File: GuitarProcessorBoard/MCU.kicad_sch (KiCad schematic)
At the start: 94 parts, among them J301 SWD Header, J302 PWR, J303 TAP, J304 MODE, J305 BYP, J306 EXP, J307 ScopeGroundLoop, SW301 RST, SW302 BOOT, U301 STM32H7B0VBT6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

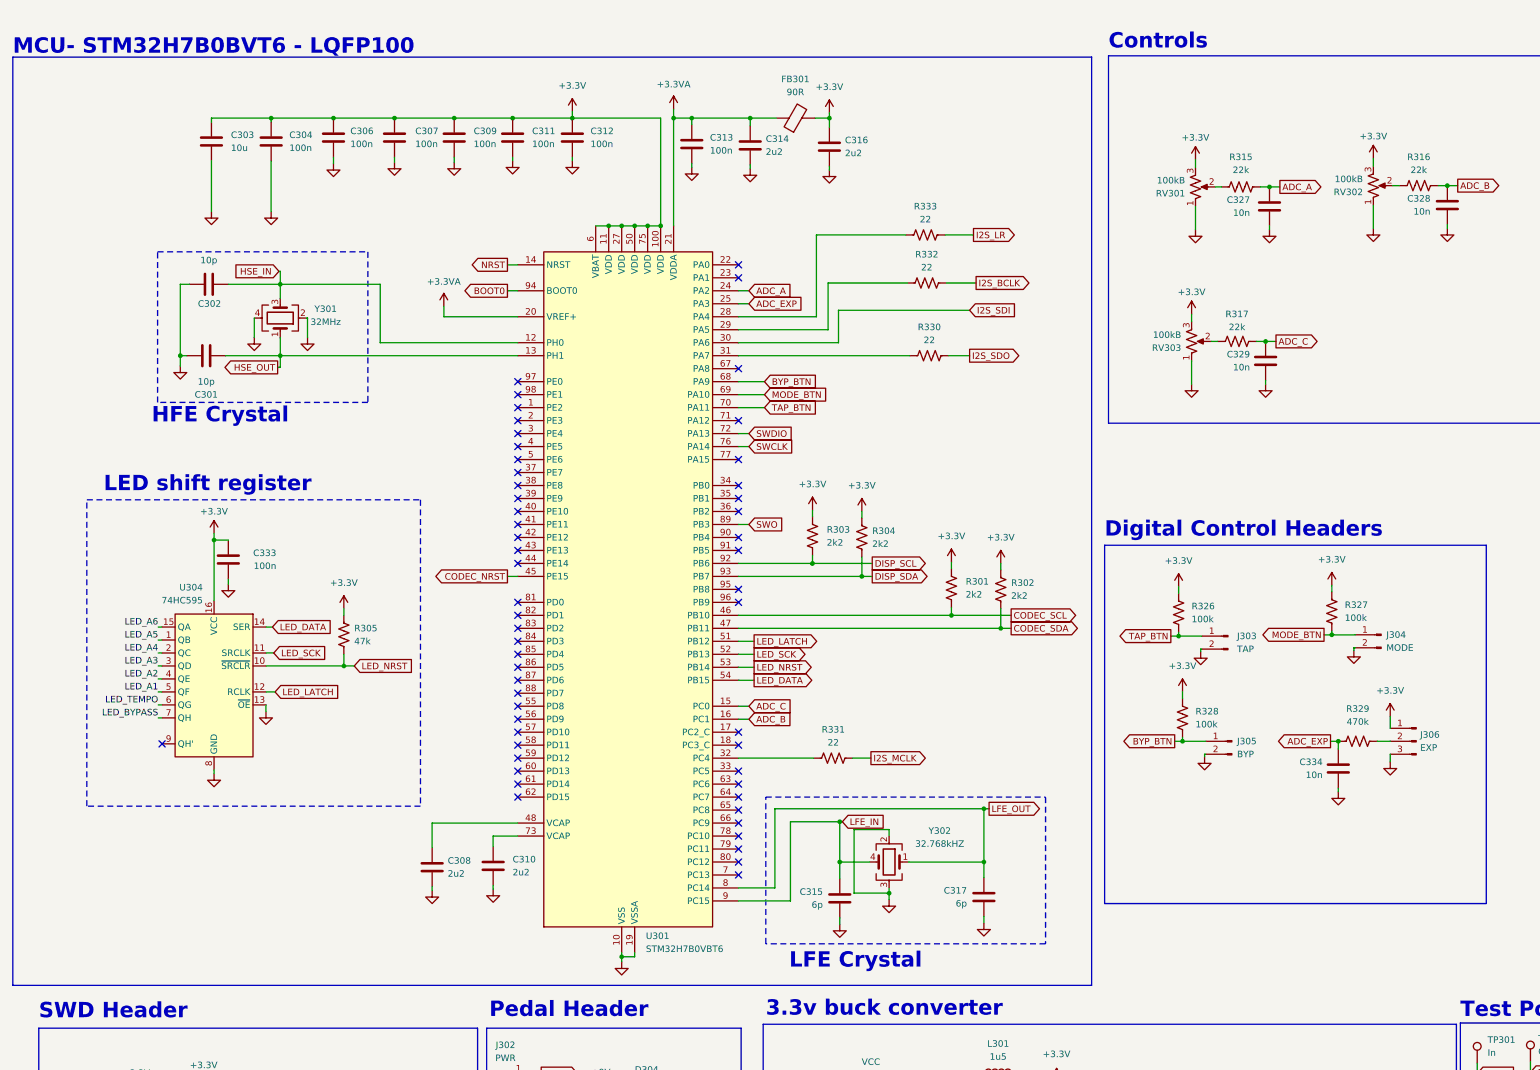
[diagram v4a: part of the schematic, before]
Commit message: differential output sim
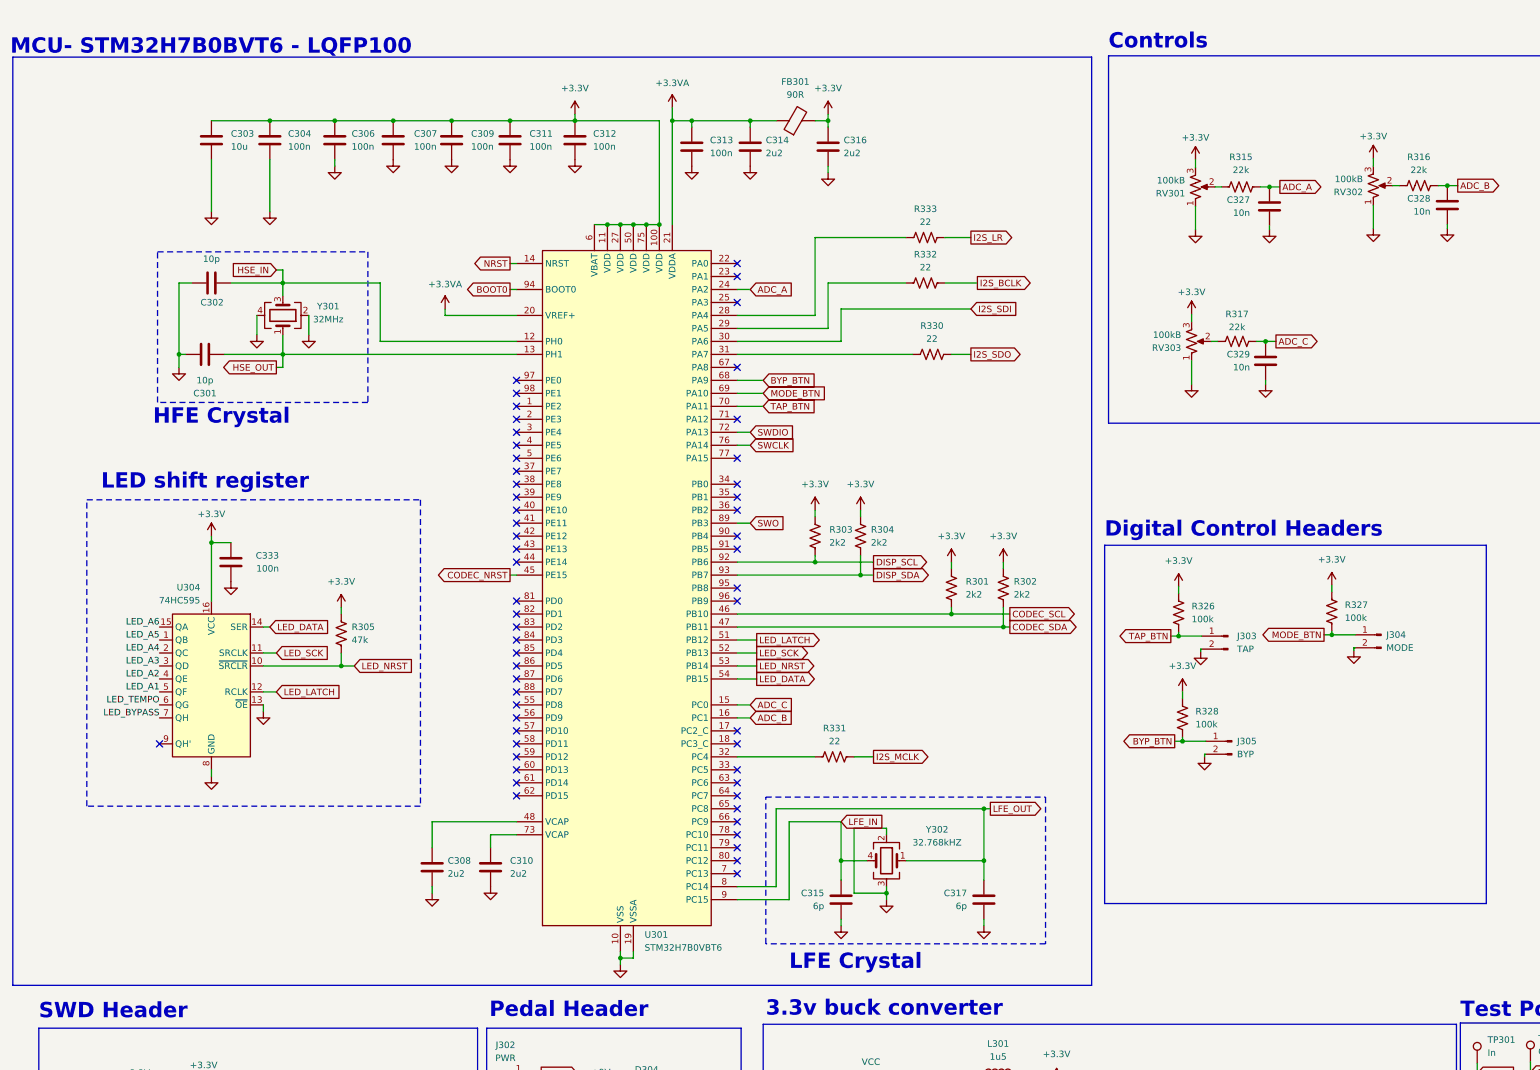
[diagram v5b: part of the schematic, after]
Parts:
- removed C334: 10n, Capacitor_SMD:C_0805_2012Metric, symbol Device:C
- removed J306: EXP, Connector_PinHeader_2.54mm:PinHeader_1x03_P2.54mm_Vertical, symbol Connector:Conn_01x03_Pin
- removed R329: 470k, Resistor_SMD:R_0805_2012Metric, symbol Device:R_US
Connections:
- net ADC_EXP: no longer names the net of U301.25 (PA3)
- no-connect marks 55 -> 56
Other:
- moved on the sheet: C302, C306, C307, C309, C310, C311, C312, C313, C317, C333, FB301, R302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

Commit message: routing start
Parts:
- removed D303: PMEG3030, Diode_SMD:D_SOD-123, symbol Device:D_Schottky
- removed J303: TAP, Connector_PinHeader_2.54mm:PinHeader_1x02_P2.54mm_Vertical, symbol Connector:Conn_01x02_Pin
- removed R326: 100k, Resistor_SMD:R_0805_2012Metric, symbol Device:R_US
- removed TP304: VCC, TestPoint:TestPoint_THTPad_D2.0mm_Drill1.0mm_VAL, symbol Connector:TestPoint
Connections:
- net +3.3V: now also J301.1 (Pin_1)
- net TAP_BTN: no longer names the net of U301.70 (PA11)
- no-connect marks 56 -> 57

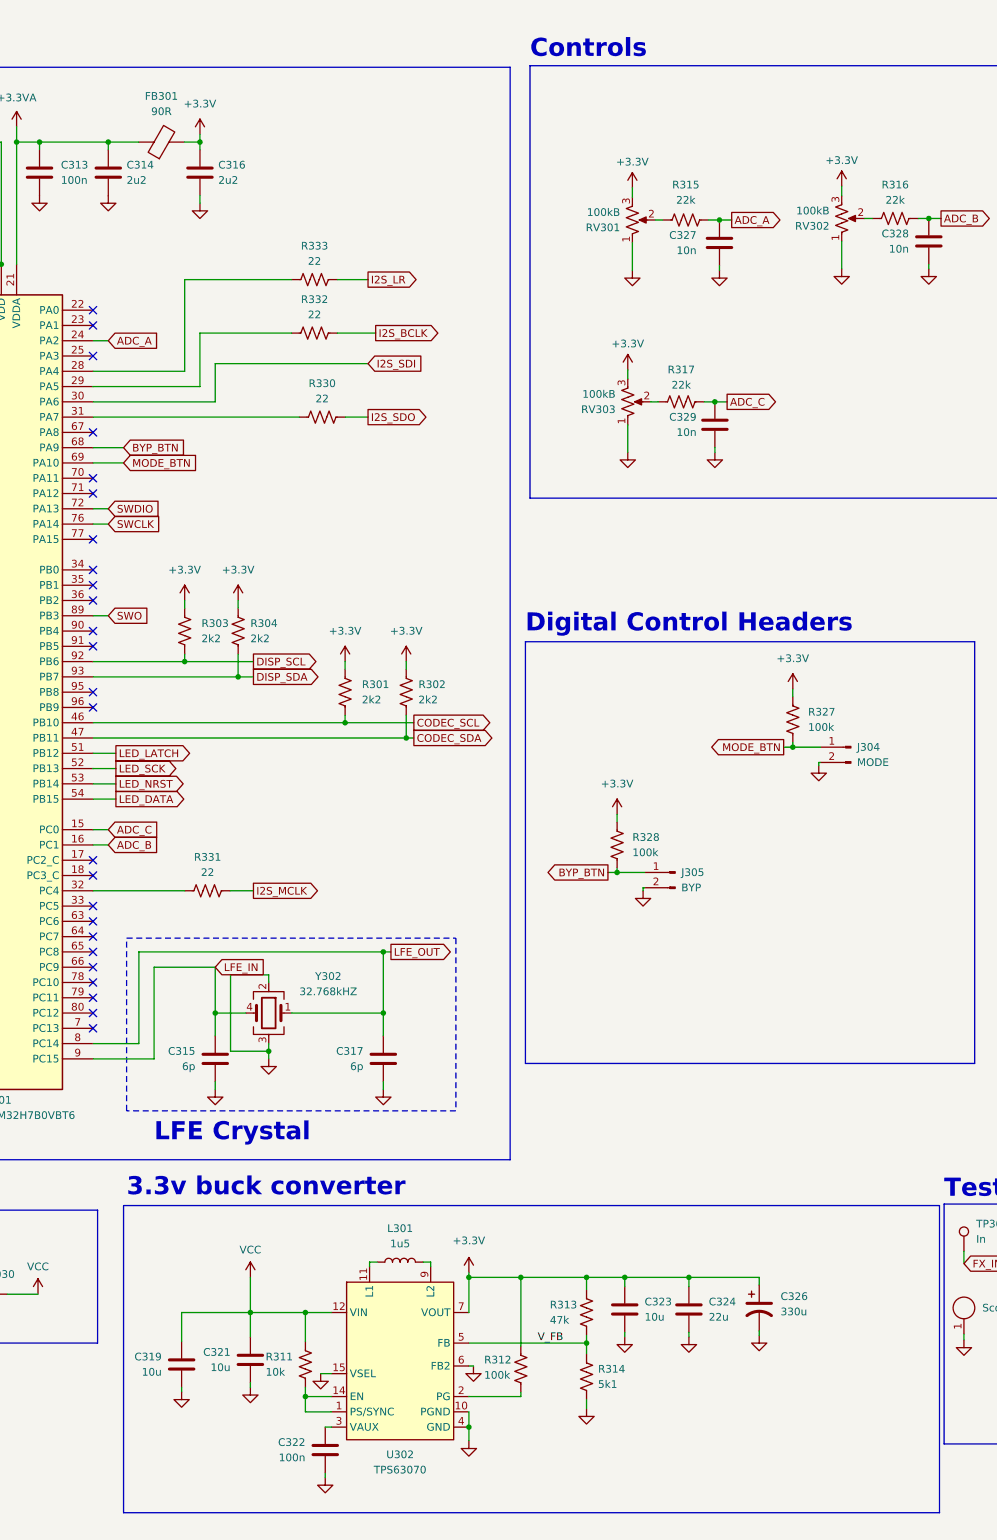
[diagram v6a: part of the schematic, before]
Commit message: more decoupling caps, return vias
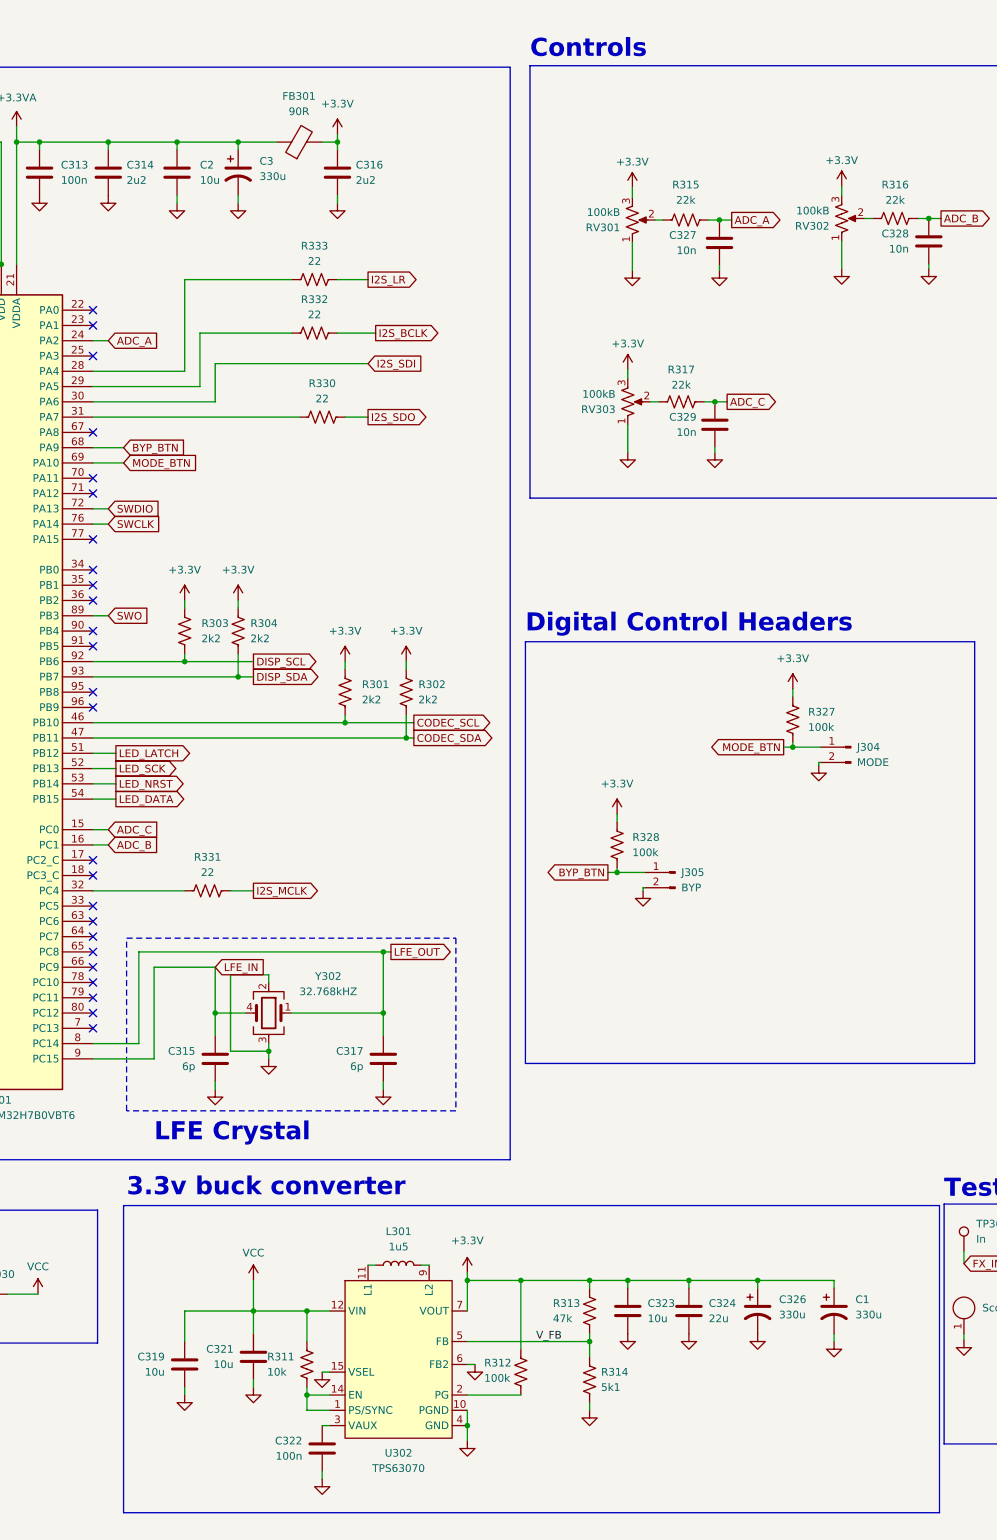
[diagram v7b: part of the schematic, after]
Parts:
- added C1, C3: 330u, Capacitor_THT:CP_Radial_D5.0mm_P2.50mm, symbol Device:C_Polarized_US
- added C2: 10u, Capacitor_SMD:C_0805_2012Metric, symbol Device:C
- U303: footprint Display:SSD1306_OLED_128x64 -> Display:SSD1306_OLED_128x64_OffBoard
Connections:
- net +3.3V: now also C1.1
- net +3.3VA: now also C2.1, C3.1
- net GND: now also C1.2, C2.2, C3.2
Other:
- moved on the sheet: C316, C319, C321, C322, C323, C326, FB301, L301, R312, R313, R314

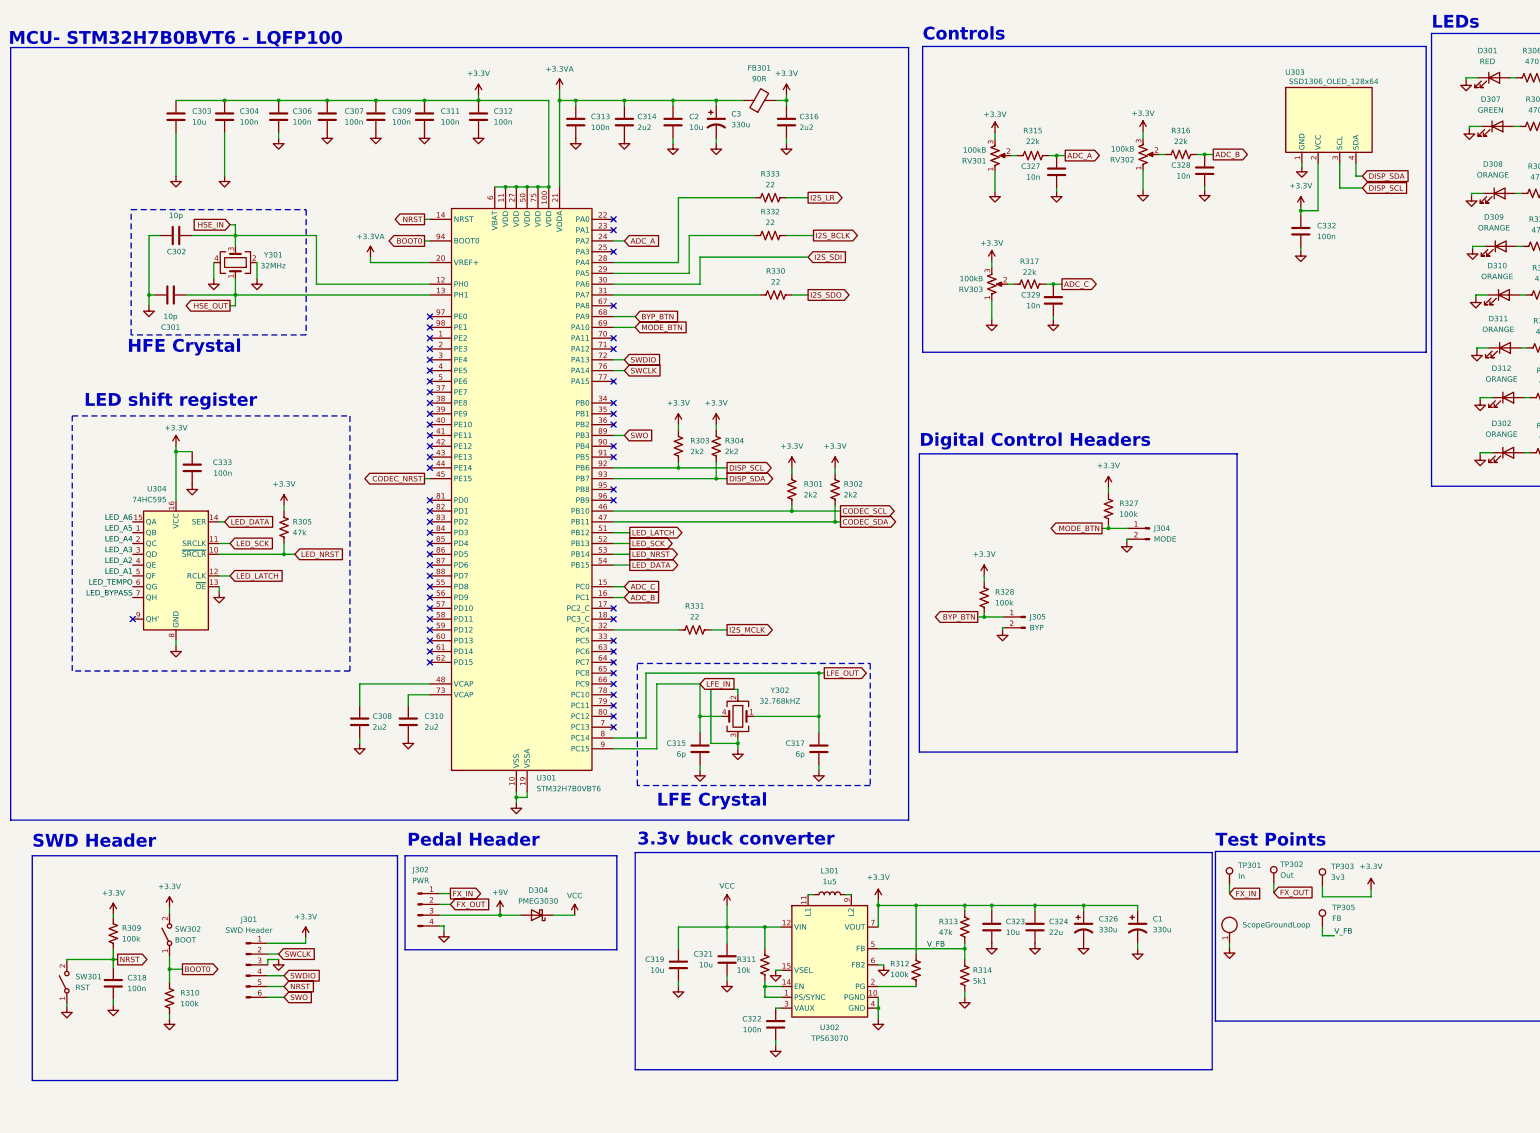
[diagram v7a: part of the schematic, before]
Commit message: split PSU schematic, DRC passing
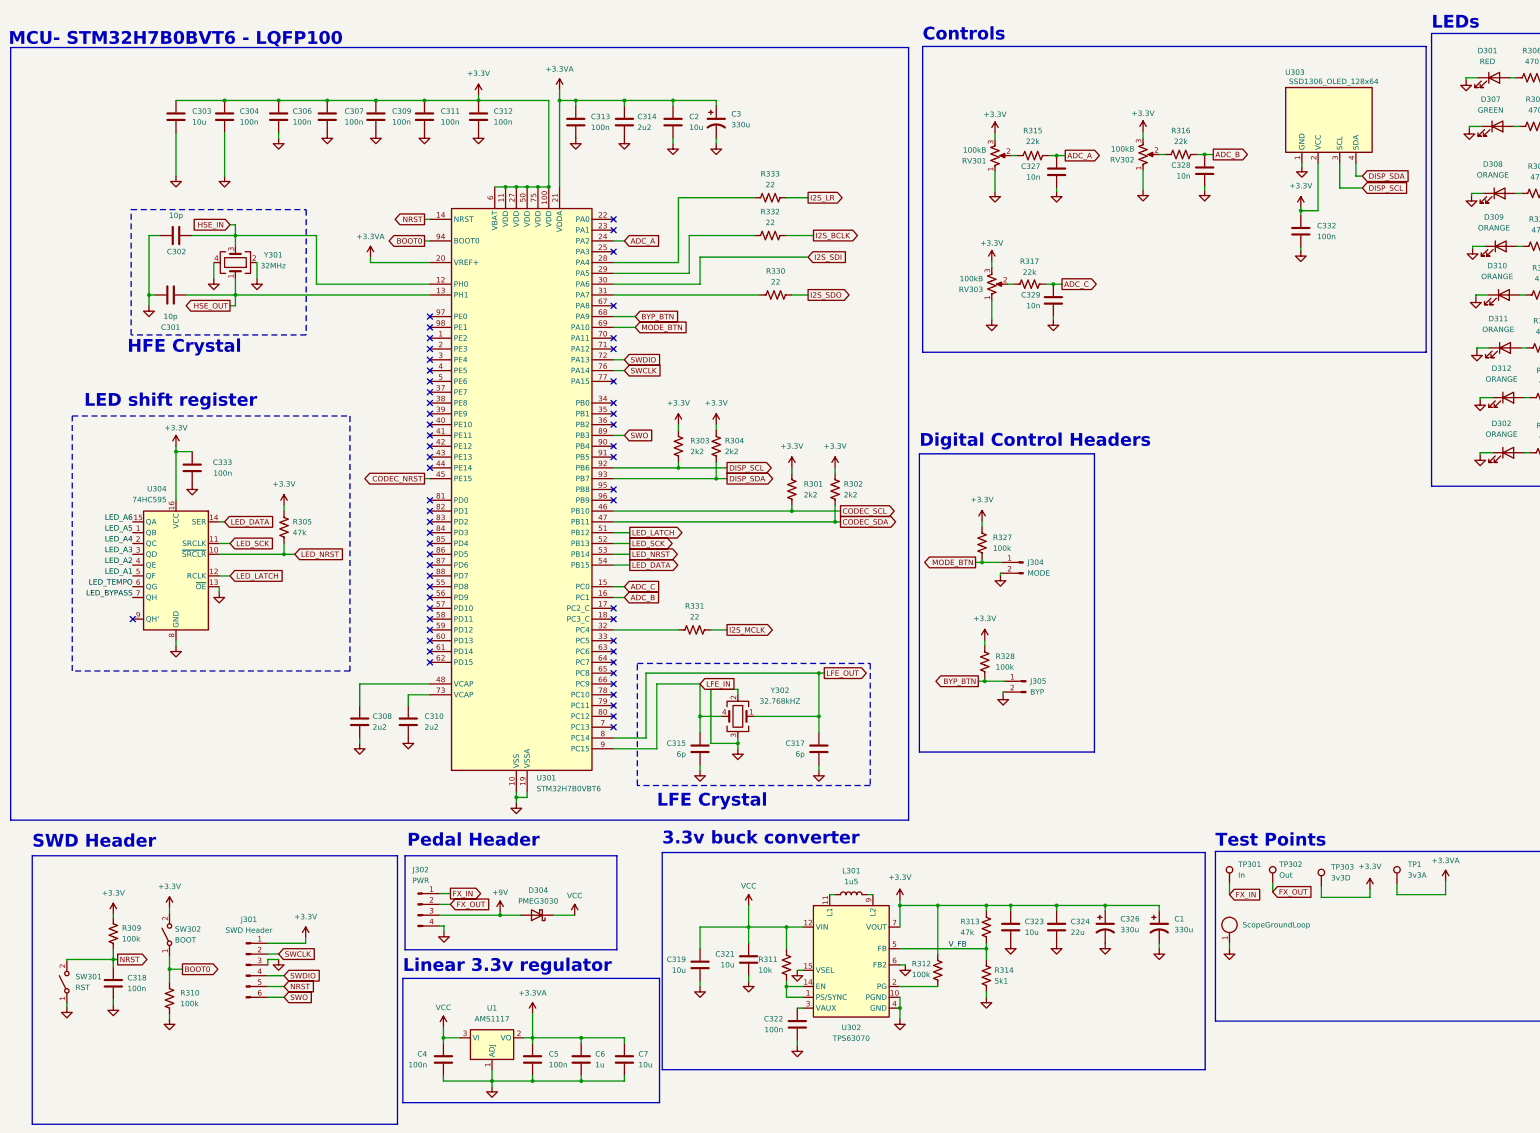
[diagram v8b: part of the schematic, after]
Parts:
- removed C316: 2u2, Capacitor_SMD:C_0805_2012Metric, symbol Device:C
- removed FB301: 90R, Resistor_SMD:R_0805_2012Metric, symbol Device:FerriteBead
- removed TP305: FB, TestPoint:TestPoint_THTPad_D2.0mm_Drill1.0mm_VAL, symbol Connector:TestPoint
- added C4, C5: 100n, Capacitor_SMD:C_0805_2012Metric, symbol Device:C
- added C6: 1u, Capacitor_SMD:C_0805_2012Metric, symbol Device:C
- added C7: 10u, Capacitor_SMD:C_0805_2012Metric, symbol Device:C
- added TP1: 3v3A, TestPoint:TestPoint_THTPad_D2.0mm_Drill1.0mm_VAL, symbol Connector:TestPoint
- added U1: AMS1117, Package_TO_SOT_SMD:SOT-223-3_TabPin2, symbol Regulator_Linear:AMS1117
- TP303: value 3v3 -> 3v3D
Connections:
- net +3.3VA: now also C5.2, C6.1, C7.1, TP1.1, U1.2 (VO)
- net GND: now also C4.1, C5.1, C6.2, C7.2, U1.1 (ADJ)
- net VCC: now also C4.2, U1.3 (VI)
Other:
- note added: "Linear 3.3v regulator"
- moved on the sheet: C1, C319, C321, C322, C323, C324, C326, J304, J305, L301, R311, R312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
